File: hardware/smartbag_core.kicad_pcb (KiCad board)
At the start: 2 copper layers, 196 x 20 mm, 24 parts, among them J1 FFC IR camera + ToF, J2 LiPo 3.7V 2000mAh, J3 Qi RX coil, J4 FSR matrix 16x6 (96 taxels), U1 SoC+NPU BLE 5.4, U2 mmWave 60GHz TRX, U3 PMIC buck-boost, U4 6-axis IMU, U5 Hall, zip, Y1 32 MHz

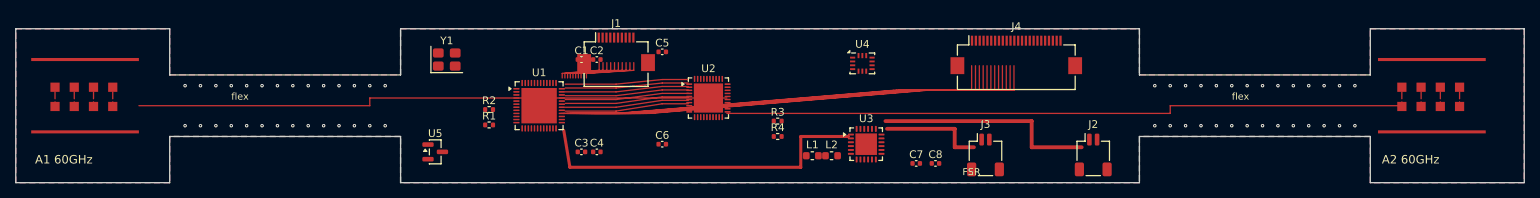
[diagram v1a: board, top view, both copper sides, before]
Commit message: Schematic with clean ERC, tested firmware core, measured recognition pipeline
The README used to open by admitting two things were missing. Both are now
there, and what is still missing is stated as a number rather than a caveat.

SCHEMATIC. Connectivity is declared once in hardware/netlist.py - pins,
electrical types and nets for 26 parts - and consumed by the schematic
generator, the board generator and the checks, so board and schematic cannot
drift. kicad-cli reports 0 ERC violations, 0 DRC violations and 0 footprint
errors on --schematic-parity.

ERC found two things genuinely missing, and they were added rather than
silenced: SWDIO/SWCLK went nowhere (there was no way to program the board, now
J5) and the SoC's ANT pin connected to nothing (a BLE radio with no antenna,
now AE1).

DRC went 439 -> 0, mostly by deleting: 224 of those violations came from the
board never declaring its process, and 214 more from the decorative routing
that existed only to make renders look like a circuit. Once the pads carried
real nets, DRC read those tracks as 40 shorts and 168 mask bridges.

The board is NOT routed. 80 unconnected pads, reported, not hidden.

FIRMWARE. The wake-up chain, the inventory ledger and the staleness rule in
portable C over injected time, with 28 host assertions under -Werror. The tests
caught three real bugs: the first closure edge eaten by the debounce, reopening
the bag ignored while settling, and MEASURE as a resting state dropping half of
forty insertions.

RECOGNITION. 1650 training images rendered through the collar module's real
optics, a ~180k-MAC embedding trained on objects the product never sees, then
five enrolled from five samples each. Closed set 0.760 single-frame, 0.817 with
the three-frame burst the firmware actually takes. Open-set rejection is 0.527
and the distributions overlap: closed-set recognition works here, "is this
something I have never seen" does not. Two identical objects swing 0.23-0.71
across splits, which is the correct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
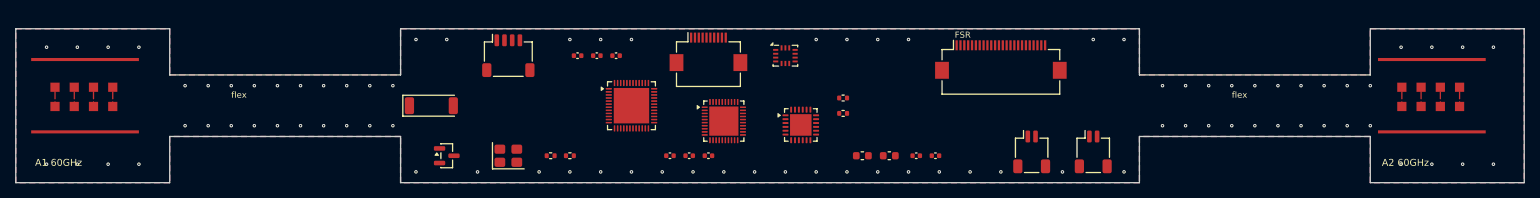
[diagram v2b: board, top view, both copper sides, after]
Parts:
- added AE1: 2.4 GHz chip antenna, RF_Antenna:Johanson_2450AT43F0100_2400-2500Mhz, F.Cu at (166.0, 148.0)
- added J5: SWD debug, Connector_JST:JST_SH_SM04B-SRSS-TB_1x04-1MP_P1.00mm_Horizontal, F.Cu at (176.0, 141.5)
- J1: value FFC IR camera + ToF -> FFC optics, 10 way
- J4: value FSR matrix 16x6 (96 taxels) -> FFC FSR matrix, 24 way
- R3: value 0R -> 10k
- moved Y1 14.8 mm to (176.0, 154.5)
- moved C5 13.9 mm to (199.5, 154.5)
- moved C3 13.3 mm to (190.0, 141.5)
- moved R2 12.1 mm to (184.0, 154.5)
- moved J1 12.0 mm to (202.0, 141.0)
- moved U1 12.0 mm to (192.0, 148.0)
- moved U4 10.0 mm to (212.0, 141.5)
- moved C4 9.51 mm to (197.0, 154.5)
- moved R3 9.01 mm to (219.5, 147.0)
- moved R4 9.01 mm to (219.5, 149.0)
- moved R1 8.94 mm to (181.5, 154.5)
- moved U3 8.86 mm to (214.0, 150.5)
- moved L2 7.50 mm to (225.5, 154.5)
- moved L1 6.50 mm to (222.0, 154.5)
- moved C6 6.18 mm to (202.0, 154.5)
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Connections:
- C1 pad 1: (no net) -> VDD_1V8
- C1 pad 2: (no net) -> GND
- C2 pad 1: (no net) -> VDD_3V3
- C2 pad 2: (no net) -> GND
- C3 pad 1: (no net) -> VDD_1V8
- C3 pad 2: (no net) -> GND
- C4 pad 1: (no net) -> VDD_3V3
- C4 pad 2: (no net) -> GND
- C5 pad 1: (no net) -> VDD_1V8
- C5 pad 2: (no net) -> GND
- C6 pad 1: (no net) -> VBAT
- C6 pad 2: (no net) -> GND
- C7 pad 1: (no net) -> VDD_3V3
- C7 pad 2: (no net) -> GND
- C8 pad 1: (no net) -> VDD_1V8
- C8 pad 2: (no net) -> GND
- J1 pad 1: (no net) -> GND
- J1 pad 10: (no net) -> GND
- J1 pad 2: (no net) -> VDD_3V3
- J1 pad 3: (no net) -> I2C_SCL
- J1 pad 4: (no net) -> I2C_SDA
- J1 pad 5: (no net) -> CAM_CLK
- J1 pad 6: (no net) -> CAM_DATA
- J1 pad 7: (no net) -> CAM_PWDN
- J1 pad 8: (no net) -> LED_PWM
- J1 pad 9: (no net) -> TOF_INT
- J2 pad 1: (no net) -> VBAT
- J2 pad 2: (no net) -> GND
- J3 pad 1: (no net) -> VQI
- J3 pad 2: (no net) -> GND
- J4 pad 1: (no net) -> GND
- J4 pad 10: (no net) -> FSR_C8
- J4 pad 11: (no net) -> FSR_C9
- J4 pad 12: (no net) -> FSR_C10
- J4 pad 13: (no net) -> FSR_C11
- J4 pad 14: (no net) -> FSR_C12
- J4 pad 15: (no net) -> FSR_C13
- J4 pad 16: (no net) -> FSR_C14
- J4 pad 17: (no net) -> FSR_C15
- J4 pad 18: (no net) -> FSR_R0
- J4 pad 19: (no net) -> FSR_R1
- J4 pad 2: (no net) -> FSR_C0
- J4 pad 20: (no net) -> FSR_R2
- J4 pad 21: (no net) -> FSR_R3
- J4 pad 22: (no net) -> FSR_R4
- J4 pad 23: (no net) -> FSR_R5
- J4 pad 24: (no net) -> GND
- J4 pad 3: (no net) -> FSR_C1
- J4 pad 4: (no net) -> FSR_C2
- J4 pad 5: (no net) -> FSR_C3
- J4 pad 6: (no net) -> FSR_C4
- J4 pad 7: (no net) -> FSR_C5
- J4 pad 8: (no net) -> FSR_C6
- J4 pad 9: (no net) -> FSR_C7
- L1 pad 1: (no net) -> SW1
- L1 pad 2: (no net) -> VDD_3V3
- L2 pad 1: (no net) -> SW2
- L2 pad 2: (no net) -> VDD_1V8
- R1 pad 1: (no net) -> nRESET
- R1 pad 2: (no net) -> VDD_3V3
- R2 pad 1: (no net) -> I2C_SDA
- R2 pad 2: (no net) -> VDD_3V3
- R3 pad 1: (no net) -> I2C_SCL
- R3 pad 2: (no net) -> VDD_3V3
- R4 pad 1: (no net) -> VBAT_SNS
- R4 pad 2: (no net) -> GND
- U1 pad 1: (no net) -> VDD_1V8
- U1 pad 10: (no net) -> BLE_ANT
- U1 pad 11: (no net) -> SPI_SCK
- U1 pad 12: (no net) -> SPI_MOSI
- U1 pad 13: (no net) -> SPI_MISO
- U1 pad 14: (no net) -> SPI_CS
- U1 pad 15: (no net) -> RADAR_IRQ
- U1 pad 16: (no net) -> I2C_SDA
- U1 pad 17: (no net) -> I2C_SCL
- U1 pad 18: (no net) -> IMU_INT
- U1 pad 19: (no net) -> HALL
- U1 pad 2: (no net) -> VDD_3V3
- U1 pad 20: (no net) -> TOF_INT
- U1 pad 21: (no net) -> CAM_CLK
- U1 pad 22: (no net) -> CAM_DATA
- U1 pad 23: (no net) -> CAM_PWDN
- U1 pad 24: (no net) -> LED_PWM
- U1 pad 25: (no net) -> VBAT_SNS
- U1 pad 26: (no net) -> PMIC_EN
- U1 pad 27: (no net) -> FSR_C0
- U1 pad 28: (no net) -> FSR_C1
- U1 pad 29: (no net) -> FSR_C2
- U1 pad 3: (no net) -> GND
- U1 pad 30: (no net) -> FSR_C3
- U1 pad 31: (no net) -> FSR_C4
- U1 pad 32: (no net) -> FSR_C5
- U1 pad 33: (no net) -> FSR_C6
- U1 pad 34: (no net) -> FSR_C7
- U1 pad 35: (no net) -> FSR_C8
- U1 pad 36: (no net) -> FSR_C9
- U1 pad 37: (no net) -> FSR_C10
- U1 pad 38: (no net) -> FSR_C11
- U1 pad 39: (no net) -> FSR_C12
- U1 pad 4: (no net) -> GND
- U1 pad 40: (no net) -> FSR_C13
- U1 pad 41: (no net) -> FSR_C14
- U1 pad 42: (no net) -> FSR_C15
- U1 pad 43: (no net) -> FSR_R0
- U1 pad 44: (no net) -> FSR_R1
- U1 pad 45: (no net) -> FSR_R2
- U1 pad 46: (no net) -> FSR_R3
- U1 pad 47: (no net) -> FSR_R4
- U1 pad 48: (no net) -> FSR_R5
- U1 pad 49: (no net) -> GND
- U1 pad 5: (no net) -> XTAL_I
- U1 pad 6: (no net) -> XTAL_O
- U1 pad 7: (no net) -> nRESET
- U1 pad 8: (no net) -> SWDIO
- U1 pad 9: (no net) -> SWCLK
- U2 pad 1: (no net) -> VDD_1V8
- U2 pad 10: (no net) -> nRESET
- U2 pad 11: (no net) -> ANT_A1
- U2 pad 12: (no net) -> ANT_A2
- U2 pad 13: (no net) -> ANT_A1
- U2 pad 14: (no net) -> ANT_A2
- U2 pad 15: (no net) -> GND
- U2 pad 16: (no net) -> GND
- U2 pad 17: (no net) -> GND
- U2 pad 18: (no net) -> GND
- U2 pad 19: (no net) -> GND
- U2 pad 2: (no net) -> VDD_1V8
- U2 pad 20: (no net) -> GND
- U2 pad 21: (no net) -> GND
- U2 pad 22: (no net) -> GND
- U2 pad 23: (no net) -> GND
- U2 pad 24: (no net) -> GND
- U2 pad 25: (no net) -> GND
- U2 pad 26: (no net) -> GND
- U2 pad 27: (no net) -> GND
- U2 pad 28: (no net) -> GND
- U2 pad 29: (no net) -> GND
- U2 pad 3: (no net) -> GND
- U2 pad 30: (no net) -> GND
- U2 pad 31: (no net) -> GND
- U2 pad 32: (no net) -> GND
- U2 pad 33: (no net) -> GND
- U2 pad 34: (no net) -> GND
- U2 pad 35: (no net) -> GND
- U2 pad 36: (no net) -> GND
- U2 pad 37: (no net) -> GND
- U2 pad 38: (no net) -> GND
- U2 pad 39: (no net) -> GND
- U2 pad 4: (no net) -> GND
- U2 pad 40: (no net) -> GND
- U2 pad 41: (no net) -> GND
- U2 pad 5: (no net) -> SPI_SCK
- U2 pad 6: (no net) -> SPI_MOSI
- U2 pad 7: (no net) -> SPI_MISO
- U2 pad 8: (no net) -> SPI_CS
- U2 pad 9: (no net) -> RADAR_IRQ
- U3 pad 1: (no net) -> VBAT
- U3 pad 10: (no net) -> GND
- U3 pad 11: (no net) -> VBAT_SNS
- U3 pad 12: (no net) -> GND
- U3 pad 13: (no net) -> GND
- U3 pad 14: (no net) -> GND
- U3 pad 15: (no net) -> GND
- U3 pad 16: (no net) -> GND
- U3 pad 17: (no net) -> GND
- U3 pad 18: (no net) -> GND
- U3 pad 19: (no net) -> GND
- U3 pad 2: (no net) -> VQI
- U3 pad 20: (no net) -> GND
- U3 pad 21: (no net) -> GND
- U3 pad 22: (no net) -> GND
- U3 pad 23: (no net) -> GND
- U3 pad 24: (no net) -> GND
- U3 pad 25: (no net) -> GND
- U3 pad 3: (no net) -> PMIC_EN
- U3 pad 4: (no net) -> SW1
- U3 pad 5: (no net) -> SW2
- U3 pad 6: (no net) -> VDD_3V3
- U3 pad 7: (no net) -> VDD_1V8
- U3 pad 8: (no net) -> VDD_3V3
- U3 pad 9: (no net) -> GND
- U4 pad 1: (no net) -> VDD_3V3
- U4 pad 10: (no net) -> GND
- U4 pad 11: (no net) -> GND
- U4 pad 12: (no net) -> GND
- U4 pad 13: (no net) -> GND
- U4 pad 14: (no net) -> GND
- U4 pad 2: (no net) -> GND
- U4 pad 3: (no net) -> I2C_SDA
- U4 pad 4: (no net) -> I2C_SCL
- U4 pad 5: (no net) -> IMU_INT
- U4 pad 6: (no net) -> VDD_3V3
- U4 pad 7: (no net) -> GND
- U4 pad 8: (no net) -> VDD_3V3
- U4 pad 9: (no net) -> GND
- U5 pad 1: (no net) -> VDD_3V3
- U5 pad 2: (no net) -> GND
- U5 pad 3: (no net) -> HALL
- Y1 pad 1: (no net) -> XTAL_I
- Y1 pad 2: (no net) -> GND
- Y1 pad 3: (no net) -> XTAL_O
- Y1 pad 4: (no net) -> GND
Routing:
- net (no net): track 1140.3 -> 0.00 mm
- net GND: vias 56 -> 87

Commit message: Taxel driver, GATT layer, companion app, RF feed and thermal budgets
Four things were outstanding: routing, the drivers and the BLE stack, the
app, and RF/thermal analysis. Three are now done and the fourth is
measured and documented rather than faked.

Two of them turned up problems the design has not answered:

- rf/feed_loss.py: the transceiver sits 87 and 99 mm from the two antenna
  islands. At 60 GHz on 0.25 mm that is 0.94 dB/cm, so 8.2 dB one way and
  16.5 dB round trip — a factor of 2.6 in radar range thrown away before
  the antenna radiates. No layout fixes it; the distance is the floorplan.
  Three architectural ways out are listed and none is chosen here.

- thermal/budget.py: sensing is thermally free (0.18 mW averaged). Qi
  charging is not — a watt of loss for two hours with the coil under the
  cell and an insulating insert wall puts the cell near 60 C against a
  45 C limit. Inverting the model gives 2.2 W as the ceiling, not 5.

Both headlines now print on every ./tools/verify.sh run, because a check
suite that only prints its passes helps to forget them.

The taxel driver is tested against the circuit rather than a mock:
test_sb_fsr.c builds and solves the nodal admittance matrix of the real
16x6 matrix. Neither scan mode the board can run is usable — floating
columns manufacture a phantom taxel at 39% of a real press, grounded
columns read real taxels 83% light. Rows at virtual ground are exact, and
cost six op-amps the netlist does not have.

The GATT layer enforces three rules instead of documenting them: no
coordinates below the confidence floor, none at all on a map that was
never measured, and a loud failure when a 198-byte inventory meets a
20-byte MTU.

The app decodes the firmware's own bytes. gen_vectors.c writes golden
payloads from the same sb_ble.c the device would run; test_protocol.mjs
decodes them and re-encodes them with the simulator's writer, asserting
the hex is identical. The simulated insert has no second data path.

Routin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
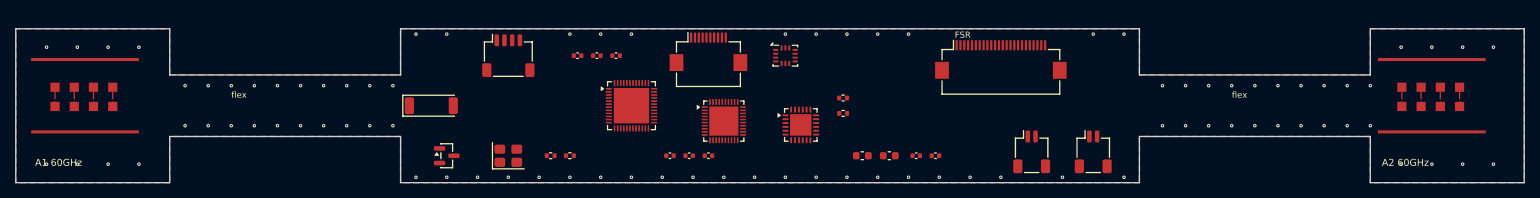
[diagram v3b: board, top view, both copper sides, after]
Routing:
- net GND: vias 87 -> 90
- added copper zone on In1.Cu, net GND
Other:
- copper layers 2 -> 4
- board text added: "A1/A2 islands: 0.25 mm dielectric under the patches, NOT 0.6"
- board text added: "full-wave sim: 0.25 mm -> -27 dB at 59.9 GHz; 0.6 mm -> -2.5 dB"

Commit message: Route the board with Freerouting; check the parts against real datasheets
KiCad has no autorouter — it was removed in v6 — so the flow is pcbnew ->
Specctra .dsn -> Freerouting -> .ses -> pcbnew. Freerouting is a maze
router with rip-up and retry, which is exactly what three hand-written
attempts had established was missing.

Routing: 699 tracks, 204 vias, 0 DRC violations, 6 unconnected pads
(was 80). In1.Cu carries zero tracks and stays a solid reference plane.

Two of the three conclusions drawn from the failed hand-written attempts
were wrong, and route.py now says so:
- "via-in-pad is mandatory at 0.4 mm pitch" is false: 204 ordinary vias,
  no via-in-pad anywhere;
- the attempts were routing to 0.2 mm tracks and 0.2 mm clearance, KiCad's
  generic netclass default, because this project declared its process
  MINIMUMS and never declared what the design uses. Half the escape
  problem was self-inflicted and DRC could not see it, because 0.2 is not
  a violation when 0.1 is merely the floor.

Three more things the router surfaced:
- an autorouter given four signal layers uses four. The first routed board
  put 34% of its tracks through the RF reference plane a comment claimed
  was never routed on. Marking the layer `power` in the DSN costs exactly
  two signals, measured.
- Specctra's boundary is the outline, so the router put a via 0.120 mm
  from an edge against a 0.150 mm rule. Moving the via afterwards landed
  it 0.089 mm from a ground pad instead; the boundary is now inset before
  the router sees it.
- a thermal spoke wider than its pad connects nothing. J1's 0.3 mm ground
  fingers had 0.4 mm spokes and sat isolated inside a ground pour.

BOM: hardware/bom.py names parts you can buy and copies package
dimensions from their datasheets; tools/bom_report.py measures the KiCad
footprints and prints the disagreements. 9 of 12 fit. The 3 that do not
are the ICs, and one of them settles an open question:

  The Acconeer A121 is a 50-ball fcCSP whose datasheet s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
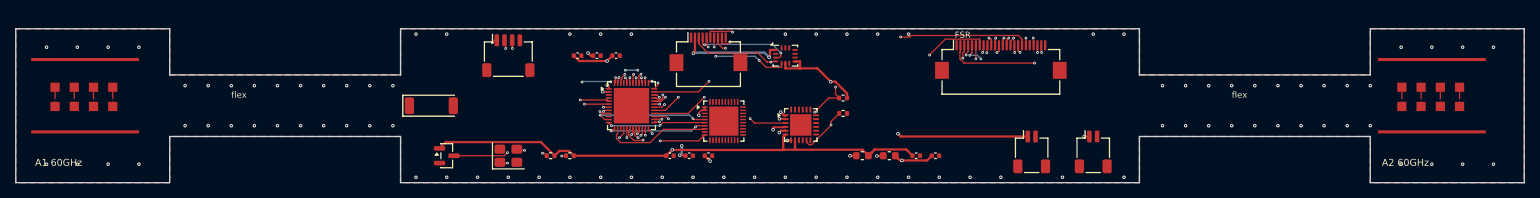
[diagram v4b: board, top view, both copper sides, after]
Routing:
- net VDD_3V3: track 0.00 -> 136.5 mm, vias 0 -> 6
- net VDD_1V8: track 0.00 -> 82.5 mm, vias 0 -> 7
- net I2C_SDA: track 0.00 -> 76.2 mm, vias 0 -> 4
- net FSR_C0: track 0.00 -> 64.5 mm, vias 0 -> 2
- net FSR_R5: track 0.00 -> 62.1 mm, vias 0 -> 2
- net FSR_R4: track 0.00 -> 61.0 mm, vias 0 -> 2
- net FSR_C15: track 0.00 -> 58.1 mm, vias 0 -> 2
- net FSR_R3: track 0.00 -> 58.1 mm, vias 0 -> 2
- net FSR_R1: track 0.00 -> 57.3 mm, vias 0 -> 4
- net I2C_SCL: track 0.00 -> 56.2 mm, vias 0 -> 4
- net FSR_C14: track 0.00 -> 55.8 mm, vias 0 -> 2
- net VBAT: track 0.00 -> 55.8 mm, vias 0 -> 3
- net FSR_R0: track 0.00 -> 55.2 mm, vias 0 -> 2
- net FSR_C12: track 0.00 -> 54.4 mm, vias 0 -> 2
- net FSR_C11: track 0.00 -> 53.1 mm, vias 0 -> 2
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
